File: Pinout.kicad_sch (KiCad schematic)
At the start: 8 parts

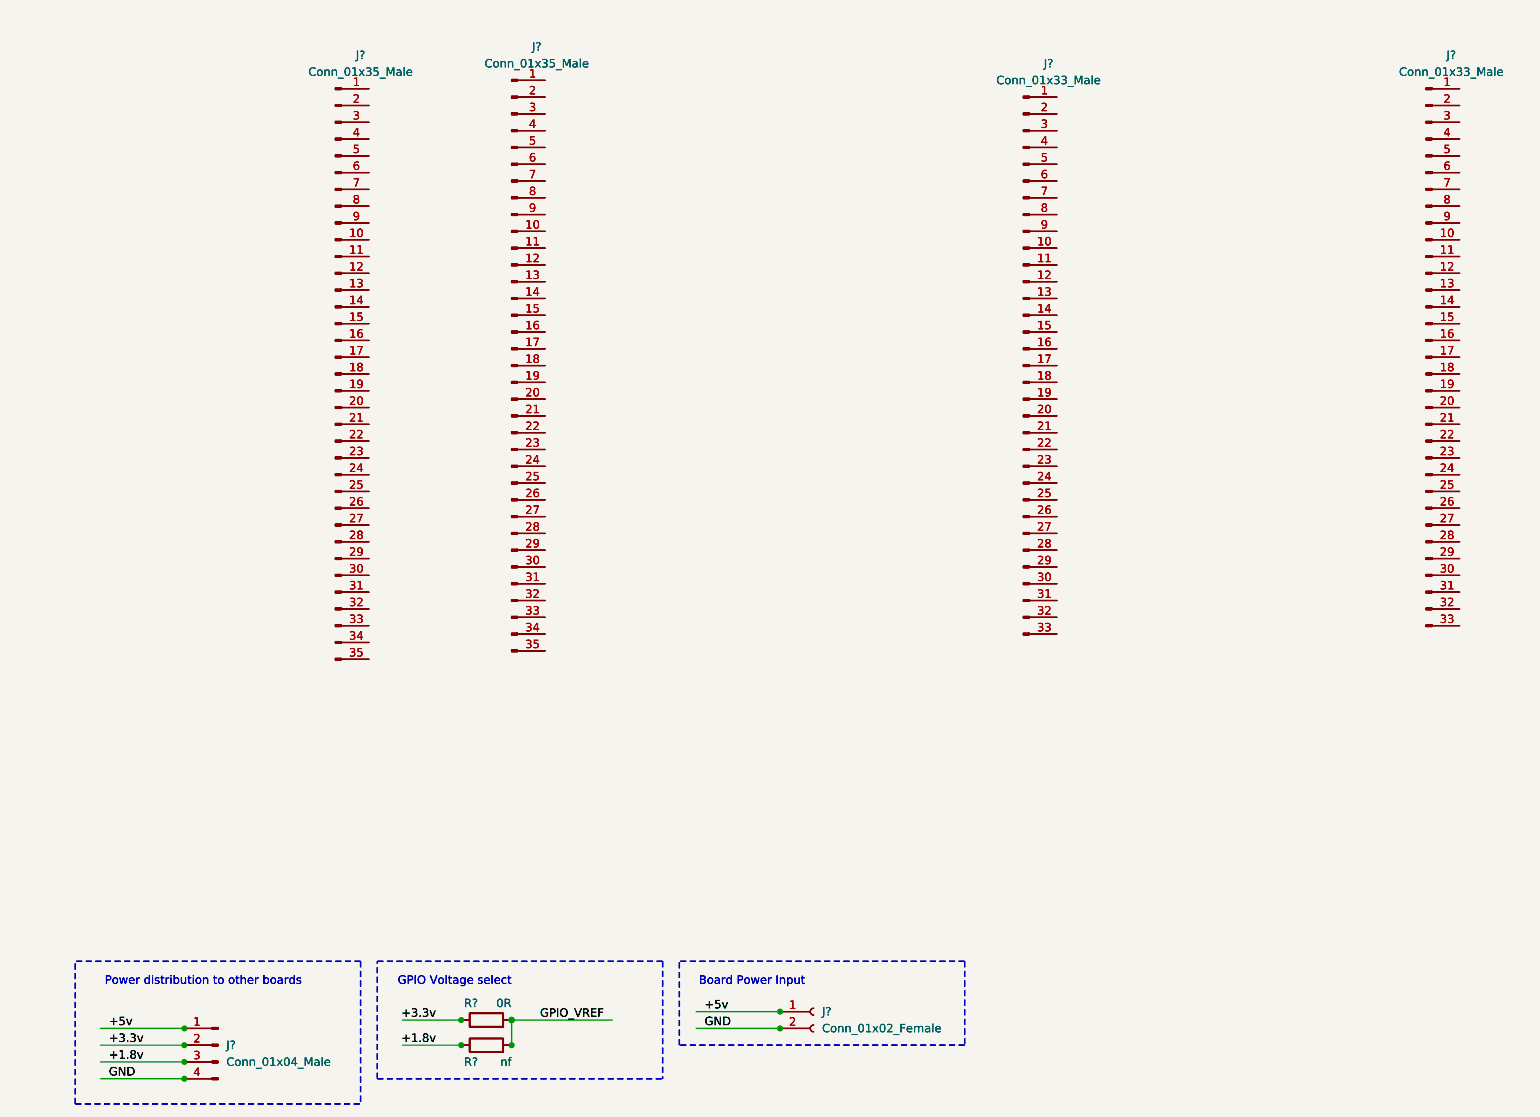
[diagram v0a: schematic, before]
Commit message: PCB ready to trace
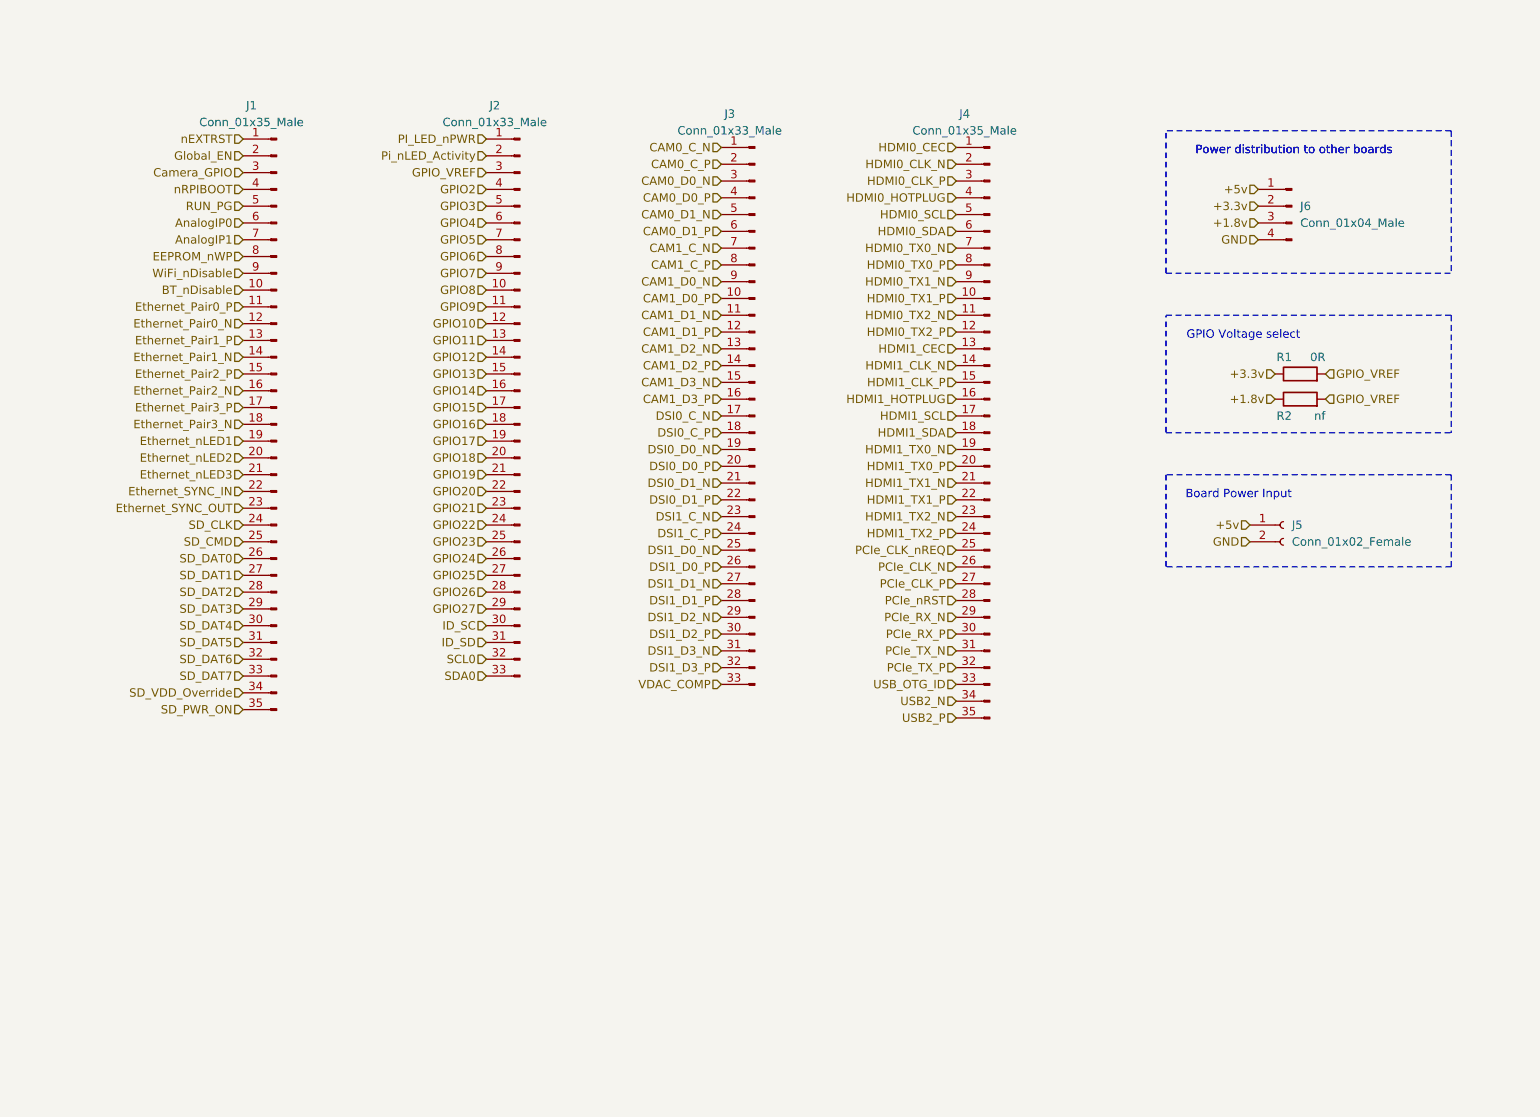
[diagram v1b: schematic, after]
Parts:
- J1, J4: renamed from J?; footprint (none) -> Connector_PinHeader_2.54mm:PinHeader_1x35_P2.54mm_Vertical
- J2, J3: renamed from J?; footprint (none) -> Connector_PinHeader_2.54mm:PinHeader_1x33_P2.54mm_Vertical
- J5: renamed from J?; footprint (none) -> Connector_PinHeader_2.54mm:PinHeader_1x02_P2.54mm_Vertical
- J6: renamed from J?; footprint (none) -> Connector_PinHeader_2.54mm:PinHeader_1x04_P2.54mm_Vertical
- R1, R2: renamed from R?; footprint Resistor_SMD:R_0805_2012Metric_Pad1.15x1.40mm_HandSolder -> Resistor_SMD:R_0805_2012Metric_Pad1.20x1.40mm_HandSolder
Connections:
- net GPIO_VREF: now also J2.3 (Pin_3)
- net CAM0_C_N: now reaches J3.1 (Pin_1)
- net CAM1_D0_P: now reaches J3.10 (Pin_10)
- net CAM1_D1_N: now reaches J3.11 (Pin_11)
- net CAM1_D1_P: now reaches J3.12 (Pin_12)
- net CAM1_D2_N: now reaches J3.13 (Pin_13)
- net CAM1_D2_P: now reaches J3.14 (Pin_14)
- net CAM1_D3_N: now reaches J3.15 (Pin_15)
- net CAM1_D3_P: now reaches J3.16 (Pin_16)
- net DSI0_C_N: now reaches J3.17 (Pin_17)
- net DSI0_C_P: now reaches J3.18 (Pin_18)
- net DSI0_D0_N: now reaches J3.19 (Pin_19)
- net CAM0_C_P: now reaches J3.2 (Pin_2)
- net DSI0_D0_P: now reaches J3.20 (Pin_20)
- net DSI0_D1_N: now reaches J3.21 (Pin_21)
- net DSI0_D1_P: now reaches J3.22 (Pin_22)
- net DSI1_C_N: now reaches J3.23 (Pin_23)
- net DSI1_C_P: now reaches J3.24 (Pin_24)
- net DSI1_D0_N: now reaches J3.25 (Pin_25)
- net DSI1_D0_P: now reaches J3.26 (Pin_26)
- net DSI1_D1_N: now reaches J3.27 (Pin_27)
- net DSI1_D1_P: now reaches J3.28 (Pin_28)
- net DSI1_D2_N: now reaches J3.29 (Pin_29)
- net CAM0_D0_N: now reaches J3.3 (Pin_3)
- net DSI1_D2_P: now reaches J3.30 (Pin_30)
- net DSI1_D3_N: now reaches J3.31 (Pin_31)
- net DSI1_D3_P: now reaches J3.32 (Pin_32)
- net VDAC_COMP: now reaches J3.33 (Pin_33)
- net CAM0_D0_P: now reaches J3.4 (Pin_4)
- net CAM0_D1_N: now reaches J3.5 (Pin_5)
- net CAM0_D1_P: now reaches J3.6 (Pin_6)
- net CAM1_C_N: now reaches J3.7 (Pin_7)
- net CAM1_C_P: now reaches J3.8 (Pin_8)
- net CAM1_D0_N: now reaches J3.9 (Pin_9)
- net nEXTRST: now reaches J1.1 (Pin_1)
- net BT_nDisable: now reaches J1.10 (Pin_10)
- net Ethernet_Pair0_P: now reaches J1.11 (Pin_11)
- net Ethernet_Pair0_N: now reaches J1.12 (Pin_12)
- net Ethernet_Pair1_P: now reaches J1.13 (Pin_13)
- net Ethernet_Pair1_N: now reaches J1.14 (Pin_14)
- net Ethernet_Pair2_P: now reaches J1.15 (Pin_15)
- net Ethernet_Pair2_N: now reaches J1.16 (Pin_16)
- net Ethernet_Pair3_P: now reaches J1.17 (Pin_17)
- net Ethernet_Pair3_N: now reaches J1.18 (Pin_18)
- net Ethernet_nLED1: now reaches J1.19 (Pin_19)
- net Global_EN: now reaches J1.2 (Pin_2)
- net Ethernet_nLED2: now reaches J1.20 (Pin_20)
- net Ethernet_nLED3: now reaches J1.21 (Pin_21)
- net Ethernet_SYNC_IN: now reaches J1.22 (Pin_22)
- net Ethernet_SYNC_OUT: now reaches J1.23 (Pin_23)
- net SD_CLK: now reaches J1.24 (Pin_24)
- net SD_CMD: now reaches J1.25 (Pin_25)
- net SD_DAT0: now reaches J1.26 (Pin_26)
- net SD_DAT1: now reaches J1.27 (Pin_27)
- net SD_DAT2: now reaches J1.28 (Pin_28)
- net SD_DAT3: now reaches J1.29 (Pin_29)
- net Camera_GPIO: now reaches J1.3 (Pin_3)
- net SD_DAT4: now reaches J1.30 (Pin_30)
- net SD_DAT5: now reaches J1.31 (Pin_31)
- net SD_DAT6: now reaches J1.32 (Pin_32)
- net SD_DAT7: now reaches J1.33 (Pin_33)
- net SD_VDD_Override: now reaches J1.34 (Pin_34)
- net SD_PWR_ON: now reaches J1.35 (Pin_35)
- net nRPIBOOT: now reaches J1.4 (Pin_4)
- net RUN_PG: now reaches J1.5 (Pin_5)
- net AnalogIP0: now reaches J1.6 (Pin_6)
- net AnalogIP1: now reaches J1.7 (Pin_7)
- net EEPROM_nWP: now reaches J1.8 (Pin_8)
- net WiFi_nDisable: now reaches J1.9 (Pin_9)
- net HDMI0_CEC: now reaches J4.1 (Pin_1)
- net HDMI0_TX1_P: now reaches J4.10 (Pin_10)
- net HDMI0_TX2_N: now reaches J4.11 (Pin_11)
- net HDMI0_TX2_P: now reaches J4.12 (Pin_12)
- net HDMI1_CEC: now reaches J4.13 (Pin_13)
- net HDMI1_CLK_N: now reaches J4.14 (Pin_14)
- net HDMI1_CLK_P: now reaches J4.15 (Pin_15)
- net HDMI1_HOTPLUG: now reaches J4.16 (Pin_16)
- net HDMI1_SCL: now reaches J4.17 (Pin_17)
- net HDMI1_SDA: now reaches J4.18 (Pin_18)
- net HDMI1_TX0_N: now reaches J4.19 (Pin_19)
- net HDMI0_CLK_N: now reaches J4.2 (Pin_2)
- net HDMI1_TX0_P: now reaches J4.20 (Pin_20)
- net HDMI1_TX1_N: now reaches J4.21 (Pin_21)
- net HDMI1_TX1_P: now reaches J4.22 (Pin_22)
- net HDMI1_TX2_N: now reaches J4.23 (Pin_23)
- net HDMI1_TX2_P: now reaches J4.24 (Pin_24)
- net PCIe_CLK_nREQ: now reaches J4.25 (Pin_25)
- net PCIe_CLK_N: now reaches J4.26 (Pin_26)
- net PCIe_CLK_P: now reaches J4.27 (Pin_27)
- net PCIe_nRST: now reaches J4.28 (Pin_28)
- net PCIe_RX_N: now reaches J4.29 (Pin_29)
- net HDMI0_CLK_P: now reaches J4.3 (Pin_3)
- net PCIe_RX_P: now reaches J4.30 (Pin_30)
- net PCIe_TX_N: now reaches J4.31 (Pin_31)
- net PCIe_TX_P: now reaches J4.32 (Pin_32)
- net USB_OTG_ID: now reaches J4.33 (Pin_33)
- net USB2_N: now reaches J4.34 (Pin_34)
- net USB2_P: now reaches J4.35 (Pin_35)
- net HDMI0_HOTPLUG: now reaches J4.4 (Pin_4)
- net HDMI0_SCL: now reaches J4.5 (Pin_5)
- net HDMI0_SDA: now reaches J4.6 (Pin_6)
- net HDMI0_TX0_N: now reaches J4.7 (Pin_7)
- net HDMI0_TX0_P: now reaches J4.8 (Pin_8)
- net HDMI0_TX1_N: now reaches J4.9 (Pin_9)
- net PI_LED_nPWR: now reaches J2.1 (Pin_1)
- net GPIO8: now reaches J2.10 (Pin_10)
- net GPIO9: now reaches J2.11 (Pin_11)
- net GPIO10: now reaches J2.12 (Pin_12)
- net GPIO11: now reaches J2.13 (Pin_13)
- net GPIO12: now reaches J2.14 (Pin_14)
- net GPIO13: now reaches J2.15 (Pin_15)
- net GPIO14: now reaches J2.16 (Pin_16)
- net GPIO15: now reaches J2.17 (Pin_17)
- net GPIO16: now reaches J2.18 (Pin_18)
- net GPIO17: now reaches J2.19 (Pin_19)
- net Pi_nLED_Activity: now reaches J2.2 (Pin_2)
- net GPIO18: now reaches J2.20 (Pin_20)
- net GPIO19: now reaches J2.21 (Pin_21)
- net GPIO20: now reaches J2.22 (Pin_22)
- net GPIO21: now reaches J2.23 (Pin_23)
- net GPIO22: now reaches J2.24 (Pin_24)
- net GPIO23: now reaches J2.25 (Pin_25)
- net GPIO24: now reaches J2.26 (Pin_26)
- net GPIO25: now reaches J2.27 (Pin_27)
- net GPIO26: now reaches J2.28 (Pin_28)
- net GPIO27: now reaches J2.29 (Pin_29)
- net ID_SC: now reaches J2.30 (Pin_30)
- net ID_SD: now reaches J2.31 (Pin_31)
- net SCL0: now reaches J2.32 (Pin_32)
- net SDA0: now reaches J2.33 (Pin_33)
- net GPIO2: now reaches J2.4 (Pin_4)
- net GPIO3: now reaches J2.5 (Pin_5)
- net GPIO4: now reaches J2.6 (Pin_6)
- net GPIO5: now reaches J2.7 (Pin_7)
- net GPIO6: now reaches J2.8 (Pin_8)
- net GPIO7: now reaches J2.9 (Pin_9)
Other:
- moved on the sheet: J1, J2, J3, J4, J5, J6, R1, R2

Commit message: Some updates to the pinout
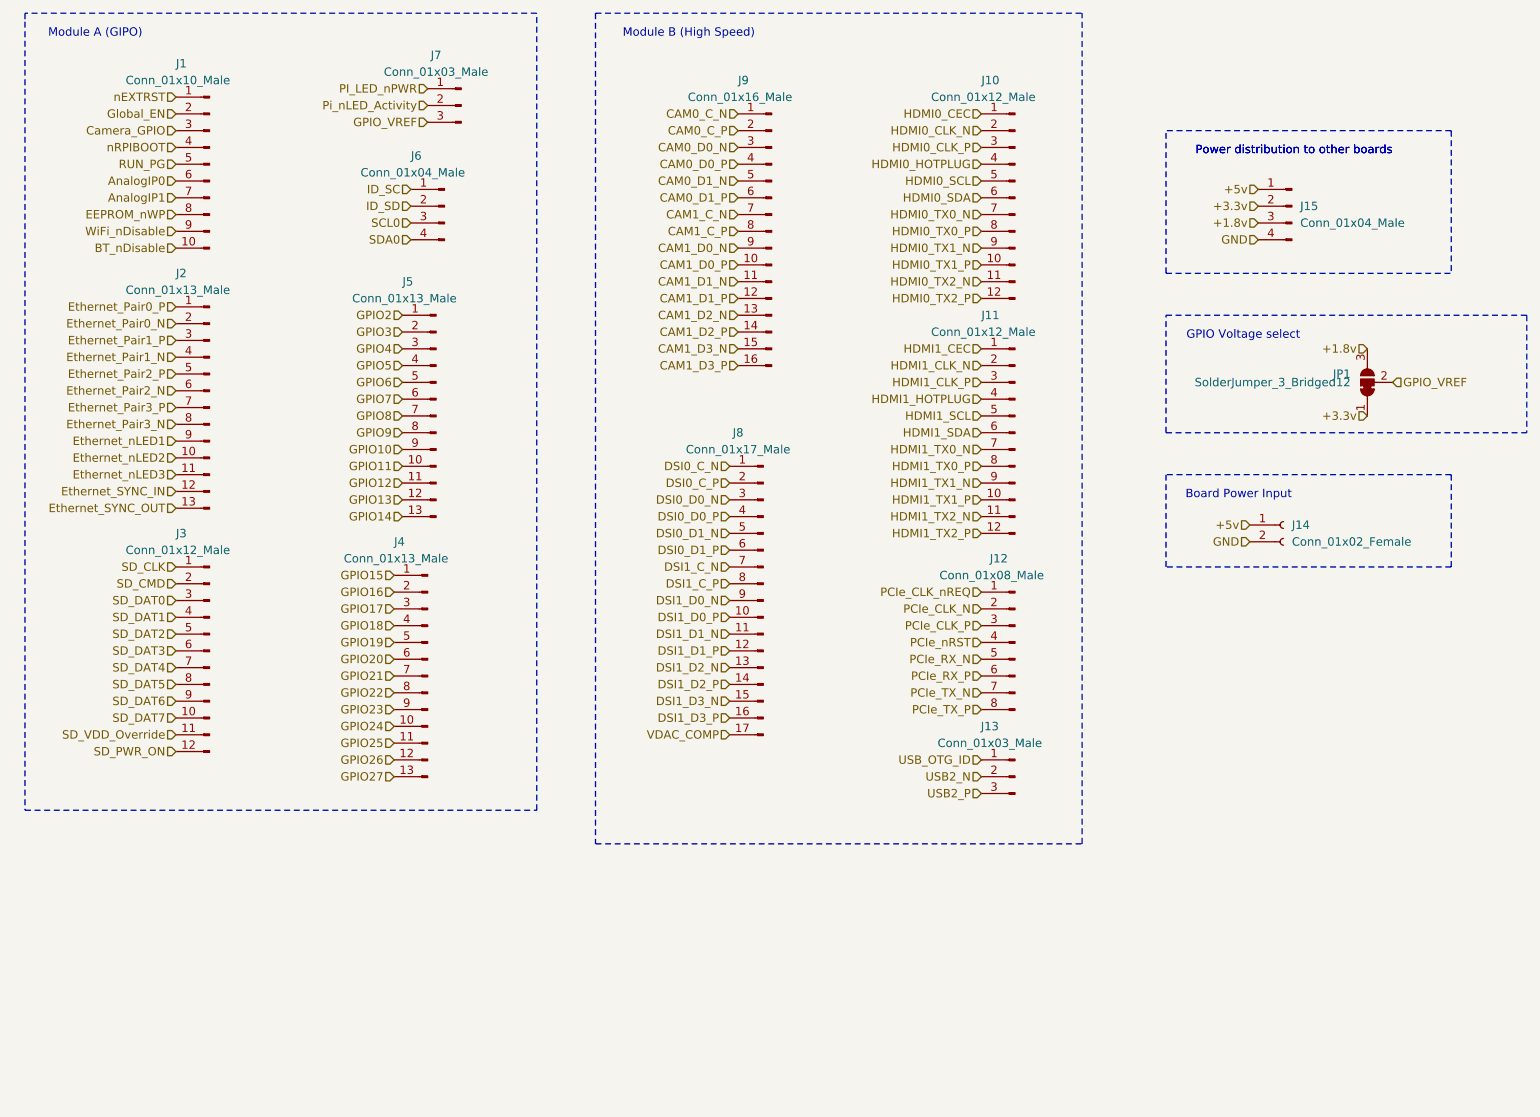
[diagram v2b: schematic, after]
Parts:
- removed J1, J4: Conn_01x35_Male, Connector_PinHeader_2.54mm:PinHeader_1x35_P2.54mm_Vertical, symbol Connector:Conn_01x35_Male
- removed J2, J3: Conn_01x33_Male, Connector_PinHeader_2.54mm:PinHeader_1x33_P2.54mm_Vertical, symbol Connector:Conn_01x33_Male
- removed R1: 0R, Resistor_SMD:R_0805_2012Metric_Pad1.20x1.40mm_HandSolder, symbol Device:R
- removed R2: nf, Resistor_SMD:R_0805_2012Metric_Pad1.20x1.40mm_HandSolder, symbol Device:R
- added J1: Conn_01x10_Male, Connector_PinHeader_2.54mm:PinHeader_1x10_P2.54mm_Vertical, symbol Connector:Conn_01x10_Male
- added J10, J11, J3: Conn_01x12_Male, Connector_PinHeader_2.54mm:PinHeader_1x12_P2.54mm_Vertical, symbol Connector:Conn_01x12_Male
- added J12: Conn_01x08_Male, Connector_PinHeader_2.54mm:PinHeader_1x08_P2.54mm_Vertical, symbol Connector:Conn_01x08_Male
- added J13, J7: Conn_01x03_Male, Connector_PinHeader_2.54mm:PinHeader_1x03_P2.54mm_Vertical, symbol Connector:Conn_01x03_Male
- added J2, J4, J5: Conn_01x13_Male, Connector_PinHeader_2.54mm:PinHeader_1x13_P2.54mm_Vertical, symbol Connector:Conn_01x13_Male
- added J6: Conn_01x04_Male, Connector_PinHeader_2.54mm:PinHeader_1x04_P2.54mm_Vertical, symbol Connector:Conn_01x04_Male
- added J8: Conn_01x17_Male, Connector_PinHeader_2.54mm:PinHeader_1x17_P2.54mm_Vertical, symbol Connector:Conn_01x17_Male
- added J9: Conn_01x16_Male, Connector_PinHeader_2.54mm:PinHeader_1x16_P2.54mm_Vertical, symbol Connector:Conn_01x16_Male
- added JP1: SolderJumper_3_Bridged12, Jumper:SolderJumper-3_P1.3mm_Bridged12_RoundedPad1.0x1.5mm, symbol Jumper:SolderJumper_3_Bridged12
- renumbered J5 to J14, J6 to J15
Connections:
- net +1.8v: now also JP1.3 (B)
- net +3.3v: now also JP1.1 (A)
- net AnalogIP0: now also J1.6 (Pin_6)
- net AnalogIP1: now also J1.7 (Pin_7)
- net BT_nDisable: now also J1.10 (Pin_10)
- net CAM0_C_N: now also J9.1 (Pin_1)
- net CAM0_C_P: now also J9.2 (Pin_2)
- net CAM0_D0_N: now also J9.3 (Pin_3)
- net CAM0_D0_P: now also J9.4 (Pin_4)
- net CAM0_D1_N: now also J9.5 (Pin_5)
- net CAM0_D1_P: now also J9.6 (Pin_6)
- net CAM1_C_N: now also J9.7 (Pin_7)
- net CAM1_C_P: now also J9.8 (Pin_8)
- net CAM1_D0_N: now also J9.9 (Pin_9)
- net CAM1_D0_P: now also J9.10 (Pin_10)
- net CAM1_D1_N: now also J9.11 (Pin_11)
- net CAM1_D1_P: now also J9.12 (Pin_12)
- net CAM1_D2_N: now also J9.13 (Pin_13)
- net CAM1_D2_P: now also J9.14 (Pin_14)
- net CAM1_D3_N: now also J9.15 (Pin_15)
- net CAM1_D3_P: now also J9.16 (Pin_16)
- net Camera_GPIO: now also J1.3 (Pin_3)
- net DSI0_C_N: now also J8.1 (Pin_1)
- net DSI0_C_P: now also J8.2 (Pin_2)
- net DSI0_D0_N: now also J8.3 (Pin_3)
- net DSI0_D0_P: now also J8.4 (Pin_4)
- net DSI0_D1_N: now also J8.5 (Pin_5)
- net DSI0_D1_P: now also J8.6 (Pin_6)
- net DSI1_C_N: now also J8.7 (Pin_7)
- net DSI1_C_P: now also J8.8 (Pin_8)
- net DSI1_D0_N: now also J8.9 (Pin_9)
- net DSI1_D0_P: now also J8.10 (Pin_10)
- net DSI1_D1_N: now also J8.11 (Pin_11)
- net DSI1_D1_P: now also J8.12 (Pin_12)
- net DSI1_D2_N: now also J8.13 (Pin_13)
- net DSI1_D2_P: now also J8.14 (Pin_14)
- net DSI1_D3_N: now also J8.15 (Pin_15)
- net DSI1_D3_P: now also J8.16 (Pin_16)
- net EEPROM_nWP: now also J1.8 (Pin_8)
- net Ethernet_Pair0_N: now also J2.2 (Pin_2)
- net Ethernet_Pair0_P: now also J2.1 (Pin_1)
- net Ethernet_Pair1_N: now also J2.4 (Pin_4)
- net Ethernet_Pair1_P: now also J2.3 (Pin_3)
- net Ethernet_Pair2_N: now also J2.6 (Pin_6)
- net Ethernet_Pair2_P: now also J2.5 (Pin_5)
- net Ethernet_Pair3_N: now also J2.8 (Pin_8)
- net Ethernet_Pair3_P: now also J2.7 (Pin_7)
- net Ethernet_SYNC_IN: now also J2.12 (Pin_12)
- net Ethernet_SYNC_OUT: now also J2.13 (Pin_13)
- net Ethernet_nLED1: now also J2.9 (Pin_9)
- net Ethernet_nLED2: now also J2.10 (Pin_10)
- net Ethernet_nLED3: now also J2.11 (Pin_11)
- net GPIO10: now also J5.9 (Pin_9)
- net GPIO11: now also J5.10 (Pin_10)
- net GPIO12: now also J5.11 (Pin_11)
- net GPIO13: now also J5.12 (Pin_12)
- net GPIO14: now also J5.13 (Pin_13)
- net GPIO15: now also J4.1 (Pin_1)
- net GPIO16: now also J4.2 (Pin_2)
- net GPIO17: now also J4.3 (Pin_3)
- net GPIO18: now also J4.4 (Pin_4)
- net GPIO19: now also J4.5 (Pin_5)
- net GPIO2: now also J5.1 (Pin_1)
- net GPIO20: now also J4.6 (Pin_6)
- net GPIO21: now also J4.7 (Pin_7)
- net GPIO22: now also J4.8 (Pin_8)
- net GPIO23: now also J4.9 (Pin_9)
- net GPIO24: now also J4.10 (Pin_10)
- net GPIO25: now also J4.11 (Pin_11)
- net GPIO26: now also J4.12 (Pin_12)
- net GPIO27: now also J4.13 (Pin_13)
- net GPIO3: now also J5.2 (Pin_2)
- net GPIO4: now also J5.3 (Pin_3)
- net GPIO5: now also J5.4 (Pin_4)
- net GPIO6: now also J5.5 (Pin_5)
- net GPIO7: now also J5.6 (Pin_6)
- net GPIO8: now also J5.7 (Pin_7)
- net GPIO9: now also J5.8 (Pin_8)
- net GPIO_VREF: now also J7.3 (Pin_3), JP1.2 (C)
- net Global_EN: now also J1.2 (Pin_2)
- net HDMI0_CEC: now also J10.1 (Pin_1)
- net HDMI0_CLK_N: now also J10.2 (Pin_2)
- net HDMI0_CLK_P: now also J10.3 (Pin_3)
- net HDMI0_HOTPLUG: now also J10.4 (Pin_4)
- net HDMI0_SCL: now also J10.5 (Pin_5)
- net HDMI0_SDA: now also J10.6 (Pin_6)
- net HDMI0_TX0_N: now also J10.7 (Pin_7)
- net HDMI0_TX0_P: now also J10.8 (Pin_8)
- net HDMI0_TX1_N: now also J10.9 (Pin_9)
- net HDMI0_TX1_P: now also J10.10 (Pin_10)
- net HDMI0_TX2_N: now also J10.11 (Pin_11)
- net HDMI0_TX2_P: now also J10.12 (Pin_12)
- net HDMI1_CEC: now also J11.1 (Pin_1)
- net HDMI1_CLK_N: now also J11.2 (Pin_2)
- net HDMI1_CLK_P: now also J11.3 (Pin_3)
- net HDMI1_HOTPLUG: now also J11.4 (Pin_4)
- net HDMI1_SCL: now also J11.5 (Pin_5)
- net HDMI1_SDA: now also J11.6 (Pin_6)
- net HDMI1_TX0_N: now also J11.7 (Pin_7)
- net HDMI1_TX0_P: now also J11.8 (Pin_8)
- net HDMI1_TX1_N: now also J11.9 (Pin_9)
- net HDMI1_TX1_P: now also J11.10 (Pin_10)
- net HDMI1_TX2_N: now also J11.11 (Pin_11)
- net HDMI1_TX2_P: now also J11.12 (Pin_12)
- net ID_SC: now also J6.1 (Pin_1)
- net ID_SD: now also J6.2 (Pin_2)
- net PCIe_CLK_N: now also J12.2 (Pin_2)
- net PCIe_CLK_P: now also J12.3 (Pin_3)
- net PCIe_CLK_nREQ: now also J12.1 (Pin_1)
- net PCIe_RX_N: now also J12.5 (Pin_5)
- net PCIe_RX_P: now also J12.6 (Pin_6)
- net PCIe_TX_N: now also J12.7 (Pin_7)
- net PCIe_TX_P: now also J12.8 (Pin_8)
- net PCIe_nRST: now also J12.4 (Pin_4)
- net PI_LED_nPWR: now also J7.1 (Pin_1)
- net Pi_nLED_Activity: now also J7.2 (Pin_2)
- net RUN_PG: now also J1.5 (Pin_5)
- net SCL0: now also J6.3 (Pin_3)
- net SDA0: now also J6.4 (Pin_4)
- net SD_CLK: now also J3.1 (Pin_1)
- net SD_CMD: now also J3.2 (Pin_2)
- net SD_DAT0: now also J3.3 (Pin_3)
- net SD_DAT1: now also J3.4 (Pin_4)
- net SD_DAT2: now also J3.5 (Pin_5)
- net SD_DAT3: now also J3.6 (Pin_6)
- net SD_DAT4: now also J3.7 (Pin_7)
- net SD_DAT5: now also J3.8 (Pin_8)
- net SD_DAT6: now also J3.9 (Pin_9)
- net SD_DAT7: now also J3.10 (Pin_10)
- net SD_PWR_ON: now also J3.12 (Pin_12)
- net SD_VDD_Override: now also J3.11 (Pin_11)
- net USB2_N: now also J13.2 (Pin_2)
- net USB2_P: now also J13.3 (Pin_3)
- net USB_OTG_ID: now also J13.1 (Pin_1)
- net VDAC_COMP: now also J8.17 (Pin_17)
- net WiFi_nDisable: now also J1.9 (Pin_9)
- net nEXTRST: now also J1.1 (Pin_1)
- net nRPIBOOT: now also J1.4 (Pin_4)
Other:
- note added: "Module A (GIPO)"
- note added: "Module B (High Speed)"
